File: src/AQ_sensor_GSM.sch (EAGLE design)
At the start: 292 parts, among them J1 F-1X03-SIP-100-32, J2 53261-0871, J4 S8411-45R, Q2 MMBT2222, Q3 MMBT2222, Q4 MMBT2222, Q5 MMBT2222, Q6 MMBT2222, Q7 MMBT2222, Q8 FS8205, T1 S8050, T2 S8050, U1 CP2102N-A02-GQFN28, U2 DS1307Z, U3 TP4056, U4 TPS63802DLAR, U5 TXS0108EPWR, U6 TPS63802DLAR, U7 TPS63802DLAR, U8 AMS1117-3.3, X1 ESP32-S3-WROOM-1-N16R8, Y1 32.768kHz

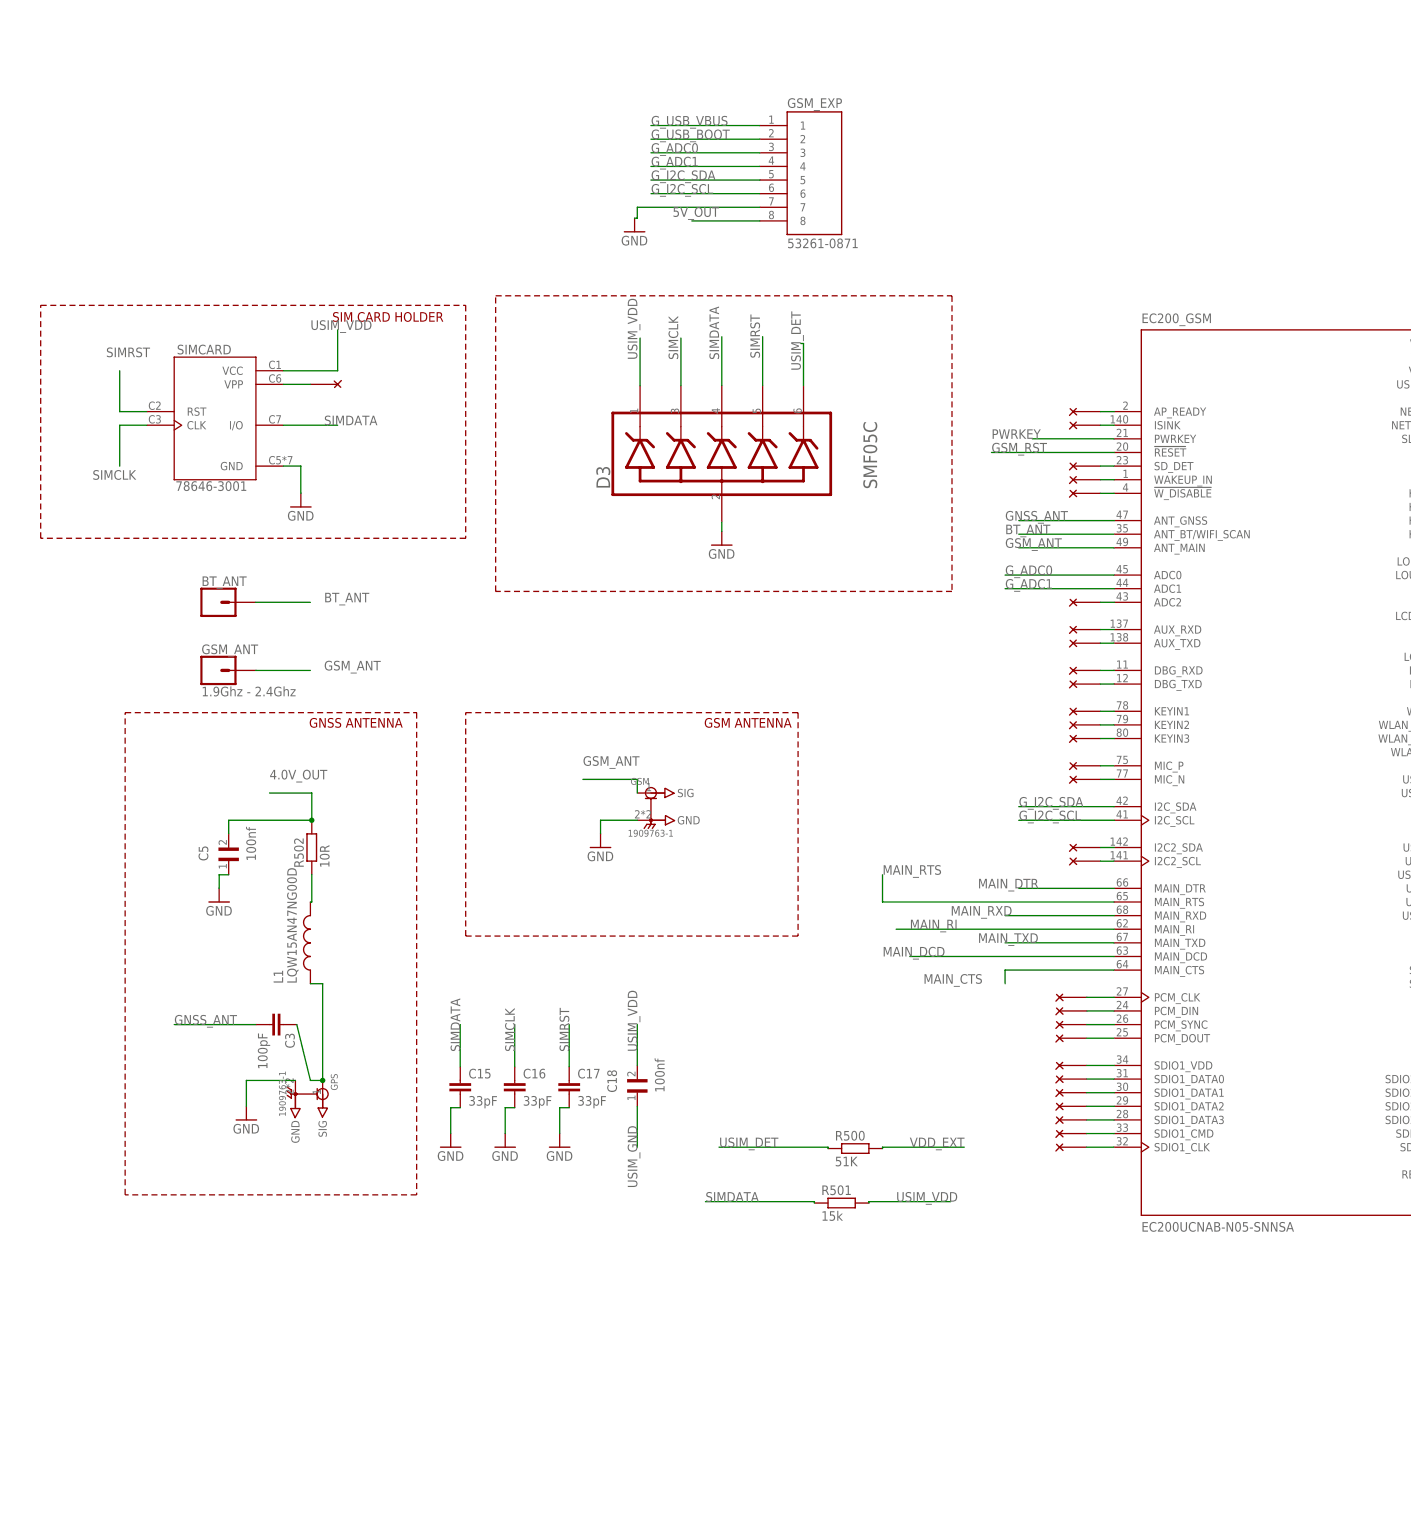
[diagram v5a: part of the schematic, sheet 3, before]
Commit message: Add 1.8V LDO, EC200UCN Firmware Boot Circuitry, GSM Patch Antenna
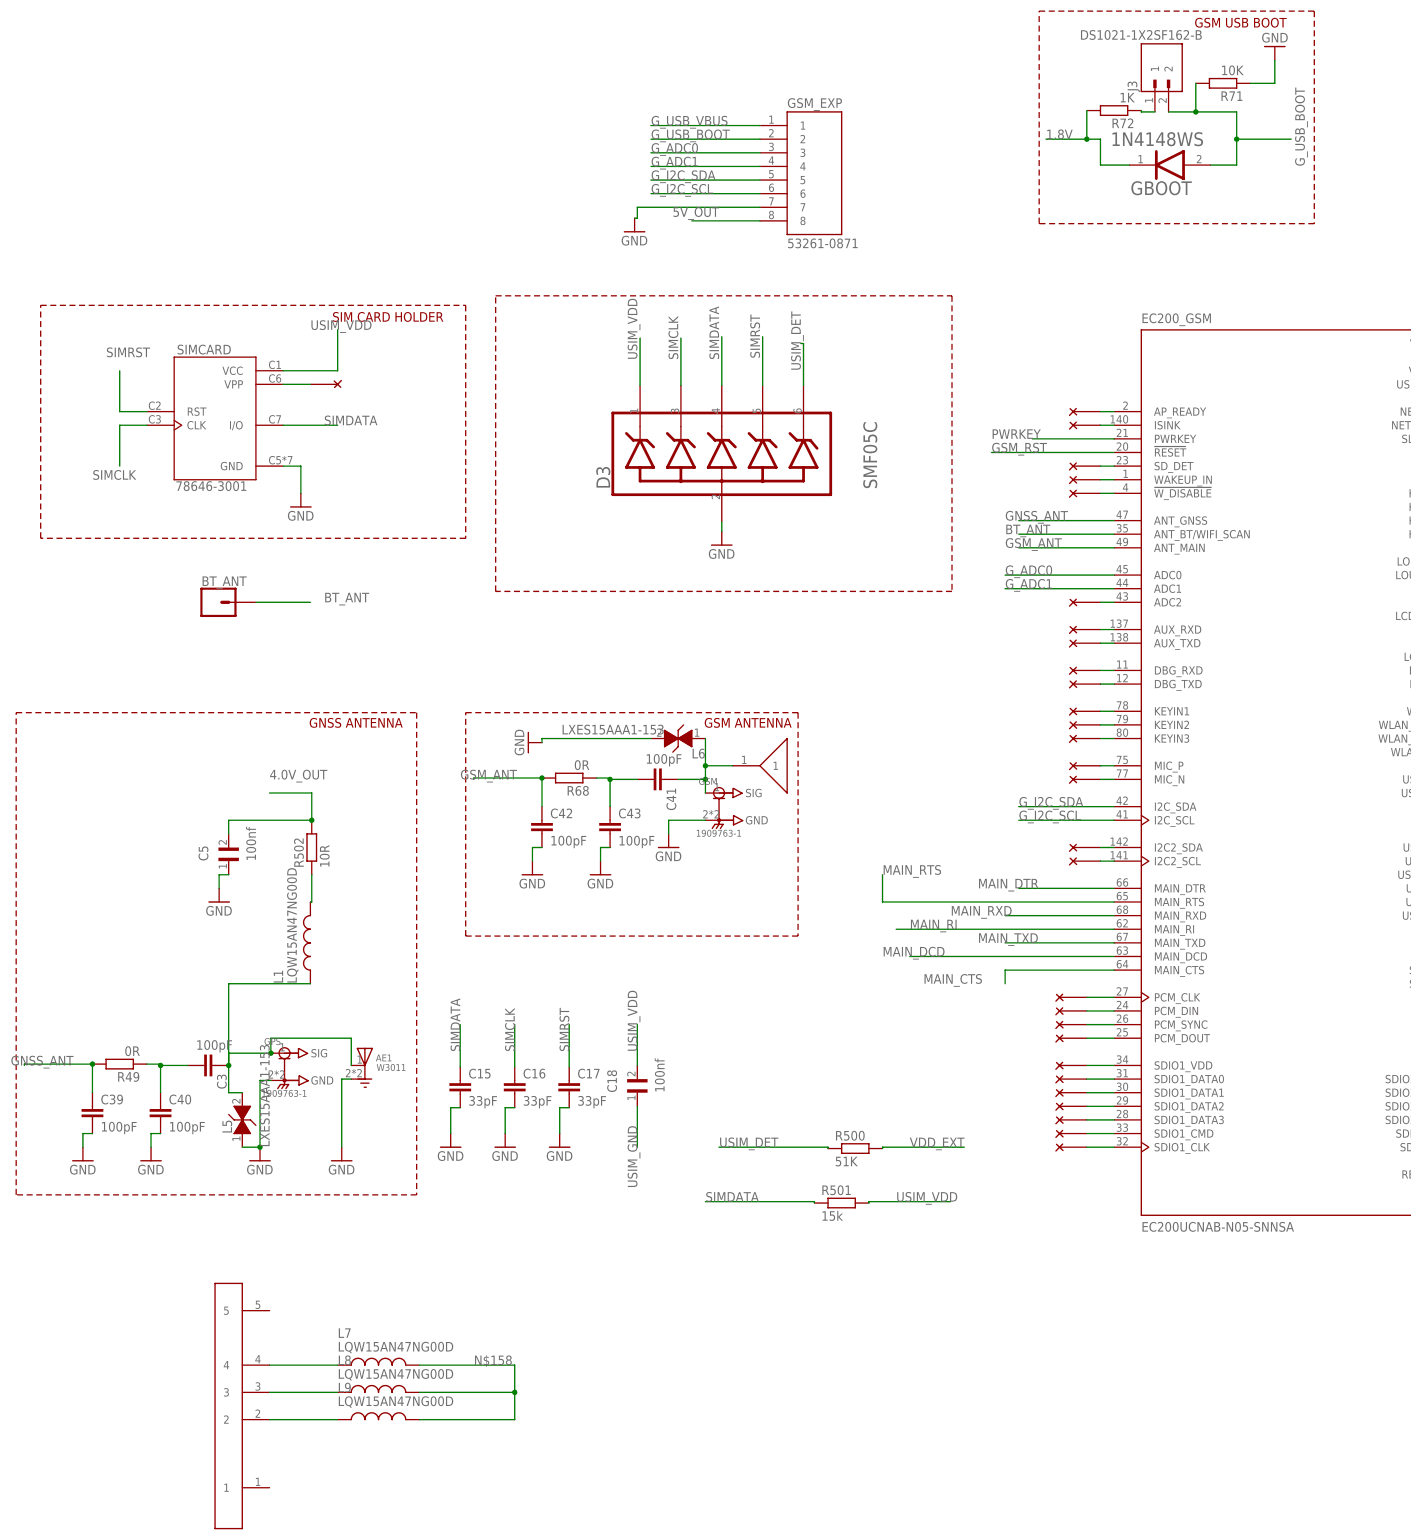
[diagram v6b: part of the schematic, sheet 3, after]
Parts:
- removed GSM_ANT: 1.9Ghz - 2.4Ghz, SparkFun-Connectors:CONN_01
- added AE1: W3011, W3011:W3011
- added C39, C40, C41, C42, C43: 100pF, SparkFun-Capacitors:100PF-0603-50V-5%
- added GBOOT: ON_SEMI_1N4148WSON_SEMI_1N4148WS_0_0, AQ_sensor_GSM:ON_SEMI_1N4148WSON_SEMI_1N4148WS_0_0
- added J3: DS1021-1X2SF162-B, DS1021-1X2SF162-B:DS1021-1X2SF162-B
- added JUMPVL1.8, R69, R70: 0.4R, Resistor_Capacitor:CRCW08050000Z0EA
- added L5, L6: LXES15AAA1-153, LXES15AAA1:LXES15AAA1-153
- added L7, L8, L9: LQW15AN47NG00D, LQW15AN47NG00D 47uh:LQW15AN47NG00D
- added R49, R68: 0R, rcl:R-EU_R0603
- added R71: 10K, rcl:R-EU_R0603
- added R72: 1K, rcl:R-EU_R0603
- added U$107: GSM_SPRING_ANTENNA, GSM_SPRING_ANTENNA:GSM_SPRING_ANTENNA
- added U$109: ADCH002_V1, ADCH002_V1:ADCH002_V1
- added U9: AMS1117-1.8, AMS1117-1.8:AMS1117-1.8
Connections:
- new net 1.8V: GBOOT.CATHODE, R70.1, R72.2
- new net N$156: C3.2, C40.1, R49.1
- new net N$157: C41.2, C43.1, R68.1
- new net N$158: C41.1, GSM.SIG, L6.1, L7.2, L8.2, L9.2, U$107.1
- new net N$161: L8.1, U$109.3
- new net N$162: L9.1, U$109.2
- new net N$163: L7.1, U$109.4
- new net N$164: JUMPVL1.8.1, R69.1, U9.VIN
- new net N$165: R70.2, U9.VOUT
- new net N$166: J3.1, R72.1
- net 5V_OUT: now also R69.2
- net GND: now also AE1.GND, C39.2, C40.2, C42.2, C43.2, L5.1, L6.2, R71.1, U9.GND/ADJ
- net GNSS_ANT: now also C39.1, R49.2; no longer C3.2
- net GSM_ANT: now also C42.1, R68.2; no longer GSM.SIG, GSM_ANT.1
- net G_USB_BOOT: now also GBOOT.ANODE, J3.2, R71.2
- net N$10: now also AE1.FEED, L5.2
- net V_LIPO: now also JUMPVL1.8.2
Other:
- note added: "GSM USB BOOT"
- moved on the sheet: C3, GPS, GSM

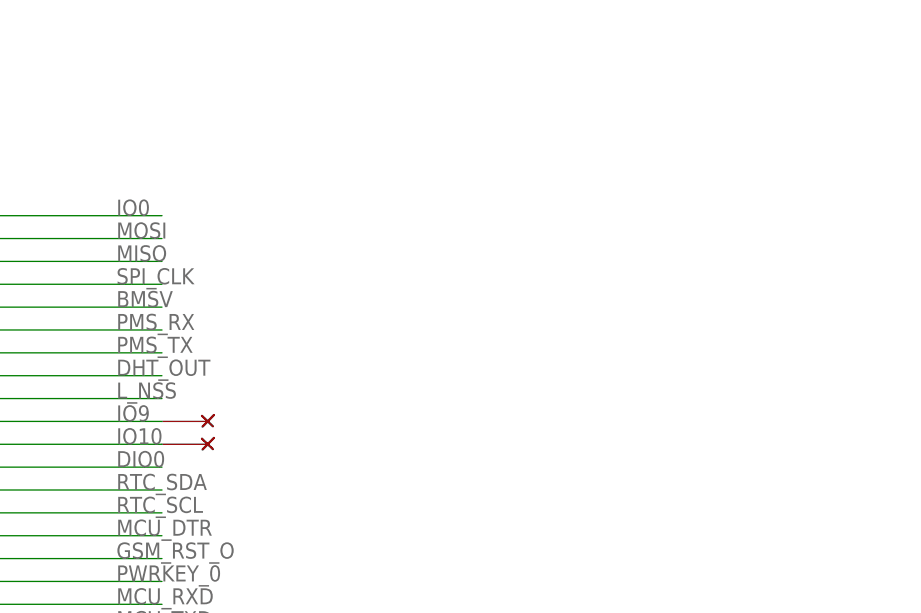
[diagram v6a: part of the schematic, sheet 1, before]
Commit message: Add Ground clearance for the antenna
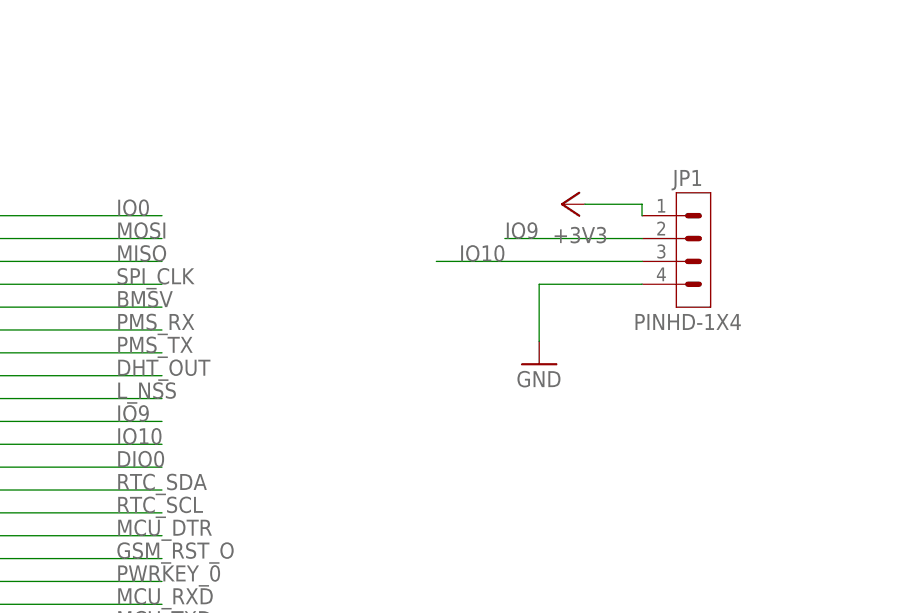
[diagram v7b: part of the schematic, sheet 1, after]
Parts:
- removed U$86, U$95: NC_MARKER, NC_MARKER:NC_MARKER
- added JP1: PINHD-1X4, Connector:PINHD-1X4
- 3.3IND: value (none) -> ORANGE
- BT_ANT: value (none) -> BTANT
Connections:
- new net N$159: R65.1, U7.EN
- net +3V3: now also JP1.1
- net BOOST_EN: no longer R65.1, U7.EN
- net GND: now also JP1.4
- net IO10: now also JP1.3; no longer U$86.P$1
- net IO9: now also JP1.2; no longer U$95.P$1
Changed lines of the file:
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@@
 <part name="GND15" library="supply1" library_urn="urn:adsk.eagle:library:371" deviceset="GND" device=""/>
 <part name="R5" library="rcl" library_urn="urn:adsk.eagle:library:334" deviceset="R-EU_" device="R0603" package3d_urn="urn:adsk.eagle:package:23555/3" value="4.7K"/>
-<part name="FRAME1" library="frames" library_urn="urn:adsk.eagle:library:229" deviceset="A3L-LOC" device=""/>
+<part name="FRAME1" library="frames" library_urn="urn:adsk.eagle:library:229" deviceset="A3L-LOC" device="" value="F1"/>
 <part name="H1" library="AQ_sensor_GSM" library_urn="urn:adsk.eagle:library:30300195" deviceset="MOUNT-PAD-ROUND" device="2.8" package3d_urn="urn:adsk.eagle:package:30300289/1"/>
 <part name="H2" library="AQ_sensor_GSM" library_urn="urn:adsk.eagle:library:30300195" deviceset="MOUNT-PAD-ROUND" device="2.8" package3d_urn="urn:adsk.eagle:package:30300289/1"/>
@@
 <part name="H4" library="AQ_sensor_GSM" library_urn="urn:adsk.eagle:library:30300195" deviceset="MOUNT-PAD-ROUND" device="2.8" package3d_urn="urn:adsk.eagle:package:30300289/1"/>
 <part name="GND61" library="supply1" library_urn="urn:adsk.eagle:library:371" deviceset="GND" device=""/>
-<part name="FRAME2" library="frames" library_urn="urn:adsk.eagle:library:229" deviceset="A3L-LOC" device=""/>
+<part name="F2" library="frames" library_urn="urn:adsk.eagle:library:229" deviceset="A3L-LOC" device=""/>
 <part name="+3V1" library="supply1" library_urn="urn:adsk.eagle:library:371" deviceset="+3V3" device=""/>
 <part name="+3V2" library="supply1" library_urn="urn:adsk.eagle:library:371" deviceset="+3V3" device=""/>
@@
 <part name="GND44" library="supply1" library_urn="urn:adsk.eagle:library:371" deviceset="GND" device=""/>
 <part name="R500" library="rcl" library_urn="urn:adsk.eagle:library:334" deviceset="R-EU_" device="R0603" package3d_urn="urn:adsk.eagle:package:23555/3" value="51K"/>
-<part name="BT_ANT" library="SparkFun-Connectors" library_urn="urn:adsk.eagle:library:513" deviceset="CONN_01" device="" package3d_urn="urn:adsk.eagle:package:38028/2"/>
+<part name="BT_ANT" library="SparkFun-Connectors" library_urn="urn:adsk.eagle:library:513" deviceset="CONN_01" device="" package3d_urn="urn:adsk.eagle:package:38028/2" value="BTANT"/>
 <part name="Q4" library="MMBT2222_" deviceset="MMBT2222*" device="" override_package3d_urn="urn:adsk.eagle:package:43001449/2" override_package_urn="urn:adsk.eagle:footprint:43001450/1"/>
 <part name="R23" library="rcl" library_urn="urn:adsk.eagle:library:334" deviceset="R-EU_" device="R0603" package3d_urn="urn:adsk.eagle:package:23555/3" value="4.7K"/>
@@
 <part name="ESP_UART" library="AQ_sensor_GSM" library_urn="urn:adsk.eagle:library:30300195" deviceset="10118192-0001LF" device="" package3d_urn="urn:adsk.eagle:package:30300275/2"/>
 <part name="GND20" library="supply1" library_urn="urn:adsk.eagle:library:371" deviceset="GND" device=""/>
-<part name="3.3IND" library="led" library_urn="urn:adsk.eagle:library:259" deviceset="LED" device="CHIP-LED0603" package3d_urn="urn:adsk.eagle:package:15819/3"/>
+<part name="3.3IND" library="led" library_urn="urn:adsk.eagle:library:259" deviceset="LED" device="CHIP-LED0603" package3d_urn="urn:adsk.eagle:package:15819/3" value="ORANGE"/>
 <part name="R7" library="rcl" library_urn="urn:adsk.eagle:library:334" deviceset="R-EU_" device="R0603" package3d_urn="urn:adsk.eagle:package:23555/3" value="200"/>
 <part name="GND31" library="supply1" library_urn="urn:adsk.eagle:library:371" deviceset="GND" device=""/>
@@
 <part name="R16" library="Resistor_Capacitor" library_urn="urn:adsk.eagle:library:15122775" deviceset="CRCW08050000Z0EA" device="" package3d_urn="urn:adsk.eagle:package:10872899/3" value="0.4R"/>
 <part name="U$75" library="NC_MARKER" deviceset="NC_MARKER" device=""/>
-<part name="U$86" library="NC_MARKER" deviceset="NC_MARKER" device=""/>
 <part name="U$87" library="NC_MARKER" deviceset="NC_MARKER" device=""/>
 <part name="U$88" library="NC_MARKER" deviceset="NC_MARKER" device=""/>
@@
 <part name="U$93" library="NC_MARKER" deviceset="NC_MARKER" device=""/>
 <part name="U$94" library="NC_MARKER" deviceset="NC_MARKER" device=""/>
-<part name="U$95" library="NC_MARKER" deviceset="NC_MARKER" device=""/>
 <part name="U$85" library="NC_MARKER" deviceset="NC_MARKER" device=""/>
 <part name="U$96" library="NC_MARKER" deviceset="NC_MARKER" device=""/>
@@
 <part name="R72" library="rcl" library_urn="urn:adsk.eagle:library:334" deviceset="R-EU_" device="R0603" package3d_urn="urn:adsk.eagle:package:23555/3" value="1K"/>
 <part name="U$107" library="GSM_SPRING_ANTENNA" deviceset="GSM_SPRING_ANTENNA" device=""/>
+<part name="JP1" library="Connector" library_urn="urn:adsk.eagle:library:16378166" deviceset="PINHD-1X4" device="" package3d_urn="urn:adsk.eagle:package:51802636/2"/>
+<part name="+3V7" library="supply1" library_urn="urn:adsk.eagle:library:371" deviceset="+3V3" device=""/>
+<part name="GND105" library="supply1" library_urn="urn:adsk.eagle:library:371" deviceset="GND" device=""/>
 </parts>
 <sheets>
@@
 <attribute name="VALUE" x="279.4" y="162.56" size="1.778" layer="96"/>
 </instance>
-<instance part="U$86" gate="G$1" x="116.84" y="137.16" smashed="yes" rot="R180"/>
 <instance part="U$87" gate="G$1" x="33.02" y="147.32" smashed="yes"/>
 <instance part="U$88" gate="G$1" x="33.02" y="144.78" smashed="yes"/>
@@
 <instance part="U$93" gate="G$1" x="33.02" y="129.54" smashed="yes"/>
 <instance part="U$94" gate="G$1" x="33.02" y="127" smashed="yes"/>
-<instance part="U$95" gate="G$1" x="116.84" y="139.7" smashed="yes" rot="R180"/>
 <instance part="U$99" gate="G$1" x="210.82" y="187.96" smashed="yes"/>
 <instance part="U$100" gate="G$1" x="210.82" y="180.34" smashed="yes"/>
@@
 <instance part="U$105" gate="G$1" x="312.42" y="223.52" smashed="yes"/>
 <instance part="U$106" gate="G$1" x="284.48" y="187.96" smashed="yes" rot="R180"/>
+<instance part="JP1" gate="A" x="170.18" y="157.48" smashed="yes">
+<attribute name="NAME" x="170.18" y="167.64" size="1.778" layer="95" align="top-center"/>
+<attribute name="VALUE" x="170.18" y="149.86" size="1.778" layer="96" align="bottom-center"/>
+</instance>
+<instance part="+3V7" gate="G$1" x="156.21" y="163.83" smashed="yes" rot="R90">
+<attribute name="VALUE" x="161.29" y="161.29" size="1.778" layer="96" rot="R180"/>
+</instance>
+<instance part="GND105" gate="1" x="153.67" y="146.05" smashed="yes">
+<attribute name="VALUE" x="151.13" y="143.51" size="1.778" layer="96"/>
+</instance>
 </instances>
 <busses>
@@
 <junction x="279.4" y="172.72"/>
 </segment>
+<segment>
+<pinref part="GND105" gate="1" pin="GND"/>
+<pinref part="JP1" gate="A" pin="4"/>
+<wire x1="153.67" y1="148.59" x2="153.67" y2="154.94" width="0.1524" layer="91"/>
+<wire x1="153.67" y1="154.94" x2="165.1" y2="154.94" width="0.1524" layer="91"/>
+</segment>
 </net>
 <net name="+3V3" class="1">
@@
 <wire x1="95.504" y1="73.66" x2="95.504" y2="79.248" width="0.1524" layer="91"/>
 </segment>
+<segment>
+<pinref part="JP1" gate="A" pin="1"/>
+<pinref part="+3V7" gate="G$1" pin="+3V3"/>
+<wire x1="165.1" y1="162.56" x2="165.1" y2="163.83" width="0.1524" layer="91"/>
+<wire x1="165.1" y1="163.83" x2="158.75" y2="163.83" width="0.1524" layer="91"/>
+</segment>
 </net>
 <net name="DHT_OUT" class="0">
@@
 <wire x1="91.44" y1="139.7" x2="111.76" y2="139.7" width="0.1524" layer="91"/>
 <label x="106.68" y="139.7" size="1.778" layer="95"/>
-<pinref part="U$95" gate="G$1" pin="P$1"/>
+</segment>
+<segment>
+<pinref part="JP1" gate="A" pin="2"/>
+<wire x1="165.1" y1="160.02" x2="149.86" y2="160.02" width="0.1524" layer="91"/>
+<label x="149.86" y="160.02" size="1.778" layer="95"/>
 </segment>
 </net>
@@
 <wire x1="91.44" y1="137.16" x2="111.76" y2="137.16" width="0.1524" layer="91"/>
 <label x="106.68" y="137.16" size="1.778" layer="95"/>
-<pinref part="U$86" gate="G$1" pin="P$1"/>
+</segment>
+<segment>
+<pinref part="JP1" gate="A" pin="3"/>
+<wire x1="165.1" y1="157.48" x2="142.24" y2="157.48" width="0.1524" layer="91"/>
+<label x="144.78" y="157.48" size="1.778" layer="95"/>
 </segment>
 </net>
@@
 </plain>
 <instances>
-<instance part="FRAME2" gate="G$1" x="0" y="0" smashed="yes">
+<instance part="F2" gate="G$1" x="0" y="0" smashed="yes">
 <attribute name="DRAWING_NAME" x="344.17" y="15.24" size="2.54" layer="94"/>
 <attribute name="LAST_DATE_TIME" x="344.17" y="10.16" size="2.286" layer="94"/>
@@
 </segment>
 </net>
-<net name="N$156" class="0">
+<net name="N$156" class="4">
 <segment>
 <pinref part="C40" gate="G$1" pin="1"/>
@@
 </segment>
 </net>
-<net name="N$10" class="0">
+<net name="N$10" class="4">
 <segment>
 <pinref part="C3" gate="G$1" pin="1"/>
@@
 <wire x1="-81.28" y1="165.1" x2="-86.36" y2="165.1" width="0.1524" layer="91"/>
 <junction x="-86.36" y="165.1"/>
+<label x="-93.98" y="162.56" size="1.778" layer="95"/>
 </segment>
 <segment>
@@
 <label x="-195.58" y="177.8" size="1.778" layer="95"/>
 </segment>
-<segment>
-<pinref part="R65" gate="G$1" pin="1"/>
-<pinref part="U7" gate="G$1" pin="EN"/>
-<wire x1="109.22" y1="259.08" x2="111.76" y2="259.08" width="0.1524" layer="91"/>
-</segment>
 </net>
 <net name="N$20" class="0">
@@
 </segment>
 </net>
+<net name="N$159" class="0">
+<segment>
+<pinref part="R65" gate="G$1" pin="1"/>
+<pinref part="U7" gate="G$1" pin="EN"/>
+<wire x1="109.22" y1="259.08" x2="111.76" y2="259.08" width="0.1524" layer="91"/>
+</segment>
+</net>
 </nets>
 </sheet>
@@
 </sheet>
 </sheets>
+<errors>
+</errors>
 </schematic>
 </drawing>
